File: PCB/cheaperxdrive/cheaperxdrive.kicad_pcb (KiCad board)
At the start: 2 copper layers, 20 parts, among them Q1 JMSL0302AG, Q2 JMSL0302AG, Q3 JMSL0302AG, Q4 JMSL0302AG, Q5 JMSL0302AG, Q6 JMSL0302AG, Q7 JMSL0302AG, Q8 JMSL0302AG, U1 STM32F405RGTx, U2 LM5109BMA, U3 DRV8301, U4 AS5047D, U5 SN65HVD232, U6 LP5907MFX-3.3, U7 AMS1117-3.3

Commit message: started schematic
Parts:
- added C1: 12p, Capacitor_SMD:C_0201_0603Metric, F.Cu at (80.6, 133.0)
- added C10: 2u2, Capacitor_SMD:C_0201_0603Metric, F.Cu at (80.6, 148.7)
- added C11: 2n2, Capacitor_SMD:C_0201_0603Metric, F.Cu at (83.0, 133.0)
- added C12: 2n2, Capacitor_SMD:C_0201_0603Metric, F.Cu at (83.0, 134.7)
- added C13: 22n, Capacitor_SMD:C_0201_0603Metric, F.Cu at (83.0, 136.5)
- added C14: 100n, Capacitor_SMD:C_0201_0603Metric, F.Cu at (83.0, 138.2)
- added C15: 100n, Capacitor_SMD:C_0201_0603Metric, F.Cu at (83.0, 140.0)
- added C16: 4u7, Capacitor_SMD:C_0201_0603Metric, F.Cu at (83.0, 141.7)
- added C17: 100n, Capacitor_SMD:C_0201_0603Metric, F.Cu at (83.0, 143.5)
- added C18: 100n, Capacitor_SMD:C_0201_0603Metric, F.Cu at (83.0, 145.2)
- added C19: 100n, Capacitor_SMD:C_0201_0603Metric, F.Cu at (83.0, 147.0)
- added C2: 12p, Capacitor_SMD:C_0201_0603Metric, F.Cu at (80.6, 134.7)
- added C20: 270p, Capacitor_SMD:C_0201_0603Metric, F.Cu at (83.0, 148.7)
- added C21: 270p, Capacitor_SMD:C_0201_0603Metric, F.Cu at (85.5, 133.0)
- added C22: 100n, Capacitor_SMD:C_0201_0603Metric, F.Cu at (85.5, 134.7)
- added C23: 4u7, Capacitor_SMD:C_0201_0603Metric, F.Cu at (85.5, 136.5)
- added C24: 12p, Capacitor_SMD:C_0201_0603Metric, F.Cu at (85.5, 138.2)
- added C25: 100n, Capacitor_SMD:C_0201_0603Metric, F.Cu at (85.5, 140.0)
- added C26: 2u2, Capacitor_SMD:C_0201_0603Metric, F.Cu at (85.5, 141.7)
- added C27: 100n, Capacitor_SMD:C_0201_0603Metric, F.Cu at (85.5, 143.5)
- added C28: 100n, Capacitor_SMD:C_0201_0603Metric, F.Cu at (85.5, 145.2)
- added C29: 4u7, Capacitor_SMD:C_0201_0603Metric, F.Cu at (85.5, 147.0)
- added C3: 2u2, Capacitor_SMD:C_0201_0603Metric, F.Cu at (80.6, 136.5)
- added C30: 2u2, Capacitor_SMD:C_0201_0603Metric, F.Cu at (85.5, 148.7)
- added C31: 4u7, Capacitor_SMD:C_0201_0603Metric, F.Cu at (87.9, 133.0)
- added C32: 4u7, Capacitor_SMD:C_0201_0603Metric, F.Cu at (87.9, 134.7)
- added C33: 100u, Capacitor_THT:CP_Radial_D5.0mm_P2.50mm, F.Cu at (64.7, 135.4)
- added C34: 100u, Capacitor_THT:CP_Radial_D5.0mm_P2.50mm, F.Cu at (64.7, 141.9)
- added C35: 100u, Capacitor_THT:CP_Radial_D5.0mm_P2.50mm, F.Cu at (64.7, 148.5)
- added C36: 100u, Capacitor_THT:CP_Radial_D5.0mm_P2.50mm, F.Cu at (64.7, 155.0)
- added C37: 100u, Capacitor_THT:CP_Radial_D5.0mm_P2.50mm, F.Cu at (64.7, 161.6)
- added C38: 4u7, Capacitor_SMD:C_0201_0603Metric, F.Cu at (87.9, 136.5)
- added C39: 4u7, Capacitor_SMD:C_0201_0603Metric, F.Cu at (87.9, 138.2)
- added C4: 2u2, Capacitor_SMD:C_0201_0603Metric, F.Cu at (80.6, 138.2)
- added C40: 4u7, Capacitor_SMD:C_0201_0603Metric, F.Cu at (87.9, 140.0)
- added C41: 2u2, Capacitor_SMD:C_0201_0603Metric, F.Cu at (87.9, 141.7)
- added C42: 100n, Capacitor_SMD:C_0201_0603Metric, F.Cu at (87.9, 143.5)
- added C43: 2u2, Capacitor_SMD:C_0201_0603Metric, F.Cu at (87.9, 145.2)
- added C44: 100n, Capacitor_SMD:C_0201_0603Metric, F.Cu at (87.9, 147.0)
- added C45: 2u2, Capacitor_SMD:C_0201_0603Metric, F.Cu at (87.9, 148.7)
- added C46: 100n, Capacitor_SMD:C_0201_0603Metric, F.Cu at (90.4, 133.0)
- added C5: 100p, Capacitor_SMD:C_0201_0603Metric, F.Cu at (80.6, 140.0)
- added C6: 270p, Capacitor_SMD:C_0201_0603Metric, F.Cu at (80.6, 141.7)
- added C7: 22n, Capacitor_SMD:C_0201_0603Metric, F.Cu at (80.6, 143.5)
- added C8: 2u2, Capacitor_SMD:C_0201_0603Metric, F.Cu at (80.6, 145.2)
- added C9: 2u2, Capacitor_SMD:C_0201_0603Metric, F.Cu at (80.6, 147.0)
- added D1: DSK310, Capacitor_SMD:C_0201_0603Metric, F.Cu at (90.4, 134.7)
- added D2: DSK310, Capacitor_SMD:C_0201_0603Metric, F.Cu at (90.4, 136.5)
- added D3: DSK310, Capacitor_SMD:C_0201_0603Metric, F.Cu at (90.4, 138.2)
- added D4: DSK310, Capacitor_SMD:C_0201_0603Metric, F.Cu at (90.4, 140.0)
- added D5: DSK310, Capacitor_SMD:C_0201_0603Metric, F.Cu at (90.4, 141.7)
- added H10: MountingHole, MountingHole:MountingHole_3.2mm_M3, F.Cu at (240.3, 70.5)
- added H11: MountingHole, MountingHole:MountingHole_3.2mm_M3, F.Cu at (184.2, 96.0)
- added H12: MountingHole, MountingHole:MountingHole_3.2mm_M3, F.Cu at (184.2, 70.5)
- added H13: MountingHole, MountingHole:MountingHole_3.2mm_M3, F.Cu at (240.3, 96.0)
- added H6: MountingHole_Pad, MountingHole:MountingHole_4.3mm_M4_Pad_Via, F.Cu at (74.3, 137.2)
- added H7: MountingHole_Pad, MountingHole:MountingHole_4.3mm_M4_Pad_Via, F.Cu at (74.3, 147.3)
- added H8: MountingHole, MountingHole:MountingHole_3.2mm_M3, F.Cu at (240.3, 121.5)
- added H9: MountingHole, MountingHole:MountingHole_3.2mm_M3, F.Cu at (184.2, 121.5)
- added J2: Conn_01x05, Connector_JST:JST_EH_B5B-EH-A_1x05_P2.50mm_Vertical, F.Cu at (108.9, 96.8)
- added J3: Conn_01x02, Connector_JST:JST_XH_B2B-XH-AM_1x02_P2.50mm_Vertical, F.Cu at (72.7, 155.8)
- added J4: Conn_01x02_Pin, Connector_PinHeader_2.54mm:PinHeader_1x02_P2.54mm_Vertical, F.Cu at (107.7, 108.2)
- added J5: Conn_01x05, Connector_JST:JST_EH_B6B-EH-A_1x06_P2.50mm_Vertical, F.Cu at (108.9, 102.7)
- added L1: 22u, Inductor_SMD:L_0201_0603Metric, F.Cu at (139.4, 74.2)
- added P1: USB_C_Plug_USB2.0, Connector_USB:USB_C_Receptacle_HRO_TYPE-C-31-M-12, F.Cu at (187.4, 108.9)
- added R1: 220k, Resistor_SMD:R_0201_0603Metric, F.Cu at (139.4, 76.0)
- added R10: 10k, Resistor_SMD:R_0201_0603Metric, F.Cu at (141.8, 77.7)
- added R11: 2R2, Resistor_SMD:R_0201_0603Metric, F.Cu at (141.8, 79.5)
- added R12: 2R2, Resistor_SMD:R_0201_0603Metric, F.Cu at (141.8, 81.2)
- added R13: 0m5, Resistor_SMD:R_0201_0603Metric, F.Cu at (141.8, 83.0)
- added R14: 2R2, Resistor_SMD:R_0201_0603Metric, F.Cu at (141.8, 84.7)
- added R15: 2R2, Resistor_SMD:R_0201_0603Metric, F.Cu at (141.8, 86.5)
- added R16: 0m5, Resistor_SMD:R_0201_0603Metric, F.Cu at (144.3, 74.2)
- added R17: 2R2, Resistor_SMD:R_0201_0603Metric, F.Cu at (144.3, 76.0)
- added R18: 2R2, Resistor_SMD:R_0201_0603Metric, F.Cu at (144.3, 77.7)
- added R19: 3k3, Resistor_SMD:R_0201_0603Metric, F.Cu at (144.3, 79.5)
- added R2: 18k, Resistor_SMD:R_0201_0603Metric, F.Cu at (139.4, 77.7)
- added R20: 2R2, Resistor_SMD:R_0201_0603Metric, F.Cu at (144.3, 81.2)
- added R21: 2R2, Resistor_SMD:R_0201_0603Metric, F.Cu at (144.3, 83.0)
- added R22: 3k3, Resistor_SMD:R_0201_0603Metric, F.Cu at (144.3, 84.7)
- added R23: 3k3, Resistor_SMD:R_0201_0603Metric, F.Cu at (144.3, 86.5)
- added R24: 3k3, Resistor_SMD:R_0201_0603Metric, F.Cu at (146.7, 74.2)
- added R25: 3k3, Resistor_SMD:R_0201_0603Metric, F.Cu at (146.7, 76.0)
- added R26: 3k3, Resistor_SMD:R_0201_0603Metric, F.Cu at (146.7, 77.7)
- added R27: 3k3, Resistor_SMD:R_0201_0603Metric, F.Cu at (146.7, 79.5)
- added R28: 3k3, Resistor_SMD:R_0201_0603Metric, F.Cu at (146.7, 81.2)
- added R29: 120, Resistor_SMD:R_0201_0603Metric, F.Cu at (146.7, 83.0)
- added R3: 18k, Resistor_SMD:R_0201_0603Metric, F.Cu at (139.4, 79.5)
- added R30: 5K1, Resistor_SMD:R_0201_0603Metric, F.Cu at (146.7, 84.7)
- added R31: 5K1, Resistor_SMD:R_0201_0603Metric, F.Cu at (146.7, 86.5)
- added R4: 3k3, Resistor_SMD:R_0201_0603Metric, F.Cu at (139.4, 81.2)
- added R5: 47k, Resistor_SMD:R_0201_0603Metric, F.Cu at (139.4, 83.0)
- added R6: 22, Resistor_SMD:R_0201_0603Metric, F.Cu at (139.4, 84.7)
- added R7: 22, Resistor_SMD:R_0201_0603Metric, F.Cu at (139.4, 86.5)
- added R8: 47k, Resistor_SMD:R_0201_0603Metric, F.Cu at (141.8, 74.2)
- added R9: 47k, Resistor_SMD:R_0201_0603Metric, F.Cu at (141.8, 76.0)
- added SW1: TS-1187A, Button_Switch_SMD:SW_SPST_CK_RS282G05A3, F.Cu at (153.4, 92.0)
- added TP1: TestPoint, TestPoint:TestPoint_Pad_D2.5mm, F.Cu at (160.4, 106.8)
- added TP2: TestPoint, TestPoint:TestPoint_Pad_D2.5mm, F.Cu at (160.4, 111.3)
- added TP3: TestPoint, TestPoint:TestPoint_Pad_D2.5mm, F.Cu at (160.4, 115.9)
- added U10: LM5109BMA, Package_SO:SOIC-8_3.9x4.9mm_P1.27mm, F.Cu at (101.2, 110.7)
- added U11: L7812, L8712:78XXS, F.Cu at (153.8, 84.6)
- added U12: USBLC6-2SC6, Package_TO_SOT_SMD:SOT-23-6, F.Cu at (134.0, 66.1)
- added U8: LM5109BMA, Package_SO:SOIC-8_3.9x4.9mm_P1.27mm, F.Cu at (101.2, 97.6)
- added U9: LM5109BMA, Package_SO:SOIC-8_3.9x4.9mm_P1.27mm, F.Cu at (101.2, 104.2)
- added Y1: 24M, Crystal:Crystal_SMD_3225-4Pin_3.2x2.5mm, F.Cu at (120.9, 110.0)
- moved H1 52.6 mm to (62.4, 119.1)
- moved H2 52.6 mm to (52.4, 119.1)
- moved H3 52.6 mm to (42.4, 119.1)
- moved H4 52.6 mm to (32.4, 119.1)
- moved H5 52.6 mm to (81.5, 108.7)
- moved Q1 52.6 mm to (62.4, 106.0)
- moved Q2 52.6 mm to (62.4, 111.7)
- moved Q3 52.6 mm to (52.4, 106.0)
- moved Q4 52.6 mm to (52.4, 111.7)
- moved Q5 52.6 mm to (42.4, 106.0)
- moved Q6 52.6 mm to (42.4, 111.7)
- moved Q7 52.6 mm to (32.4, 106.0)
- moved Q8 52.6 mm to (32.4, 111.7)
- moved U1 52.6 mm to (63.4, 84.0)
- moved U4 52.6 mm to (49.9, 95.9)
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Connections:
- U1 pad 12: unconnected-(U1-VSSA-Pad12) -> GND
- U1 pad 17: unconnected-(U1-PA3-Pad17) -> /GPIO4
- U1 pad 18: Net-(U1-VSS-Pad18) -> GND
- U1 pad 63: Net-(U1-VSS-Pad18) -> GND
- U1 pad 7: Net-(U1-NRST) -> /SYS_RST
- U5 pad 3: Net-(U5-VCC) -> +3V3
- U5 pad 6: unconnected-(U5-CANL-Pad6) -> /CAN_L
- U5 pad 7: unconnected-(U5-CANH-Pad7) -> /CAN_H
- U7 pad 3: unconnected-(U7-VI-Pad3) -> +5V
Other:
- board outline added: 63 x 58 mm

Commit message: finished first layer, may rework
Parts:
- C1, C10, C11, C12, C13, C14, C15, C16, C17, C18, C19, C2, C20, C21, C22, C23, C24, C27, C3, C4, C5, C6, C8, C9, D1, L1, R1, R19, R22, R3, R5, R8, R9, U1, U10, U2, U3, U4, U8, U9, Y1: moved to B.Cu
- moved H4 206.3 mm to (237.8, 99.3)
- moved Q8 195.3 mm to (226.8, 92.1)
- moved Q7 191.3 mm to (222.5, 84.6)
- moved H7 173.9 mm to (231.9, 73.7), turned to 90 degrees
- moved U3 168.3 mm to (200.5, 87.0), turned to -90 degrees
- moved C33 163.5 mm to (224.4, 100.6), turned to -90 degrees
- moved U4 162.4 mm to (212.3, 96.0), turned to 180 degrees
- moved H6 160.5 mm to (221.8, 73.7), turned to 90 degrees
- moved U1 158.9 mm to (222.3, 86.3), turned to 180 degrees
- moved C34 158.7 mm to (217.9, 100.6), turned to -90 degrees
- moved H5 157.6 mm to (237.8, 87.9)
- moved Q1 156.6 mm to (218.4, 92.2), turned to 0 degrees
- moved Q3 156.6 mm to (208.4, 92.2), turned to 0 degrees
- moved Q5 156.6 mm to (198.4, 92.2), turned to 0 degrees
- moved H1 156.5 mm to (212.2, 73.7)
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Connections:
- H6 pad 1: VDD -> VPP
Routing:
- net VPP: track 0.00 -> 126.5 mm
- net GND: track 0.00 -> 104.4 mm, vias 0 -> 7
- net /0SH_A: track 0.00 -> 26.3 mm, vias 0 -> 1
- net /0SH_C: track 0.00 -> 24.1 mm, vias 0 -> 1
- net /0SH_B: track 0.00 -> 23.9 mm, vias 0 -> 1
- net /USB_VBUS: track 0.00 -> 23.4 mm
- net /USB_P: track 0.00 -> 19.8 mm
- net +5V: track 0.00 -> 18.4 mm, vias 0 -> 1
- net /SH_AUX: track 0.00 -> 18.1 mm
- net +3V3: track 0.00 -> 17.7 mm, vias 0 -> 1
- net /CAN_L: track 0.00 -> 17.5 mm
- net /USB_N: track 0.00 -> 15.9 mm
- net /CAN_H: track 0.00 -> 13.8 mm
- net Net-(P1-CC1): track 0.00 -> 10.2 mm
- net Net-(P1-CC2): track 0.00 -> 9.28 mm
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- added copper zone on F.Cu, net GND

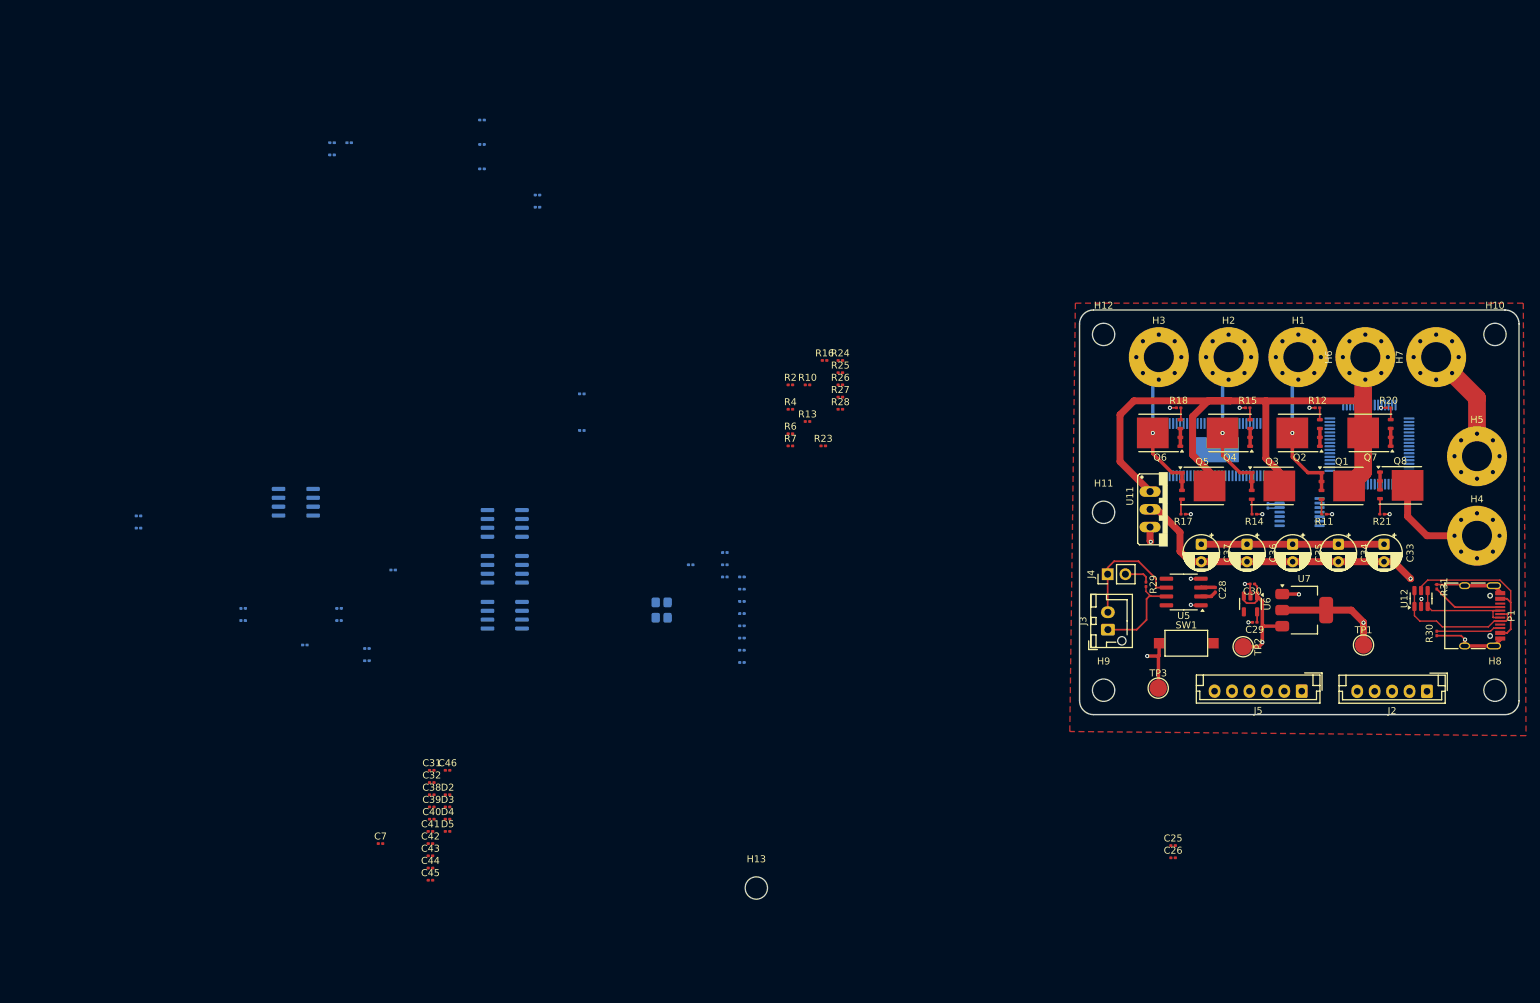
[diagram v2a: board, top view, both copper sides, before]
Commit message: pausing pcb work for now, corrected schematic to remove redundant gate drivers and removed 5v ldo
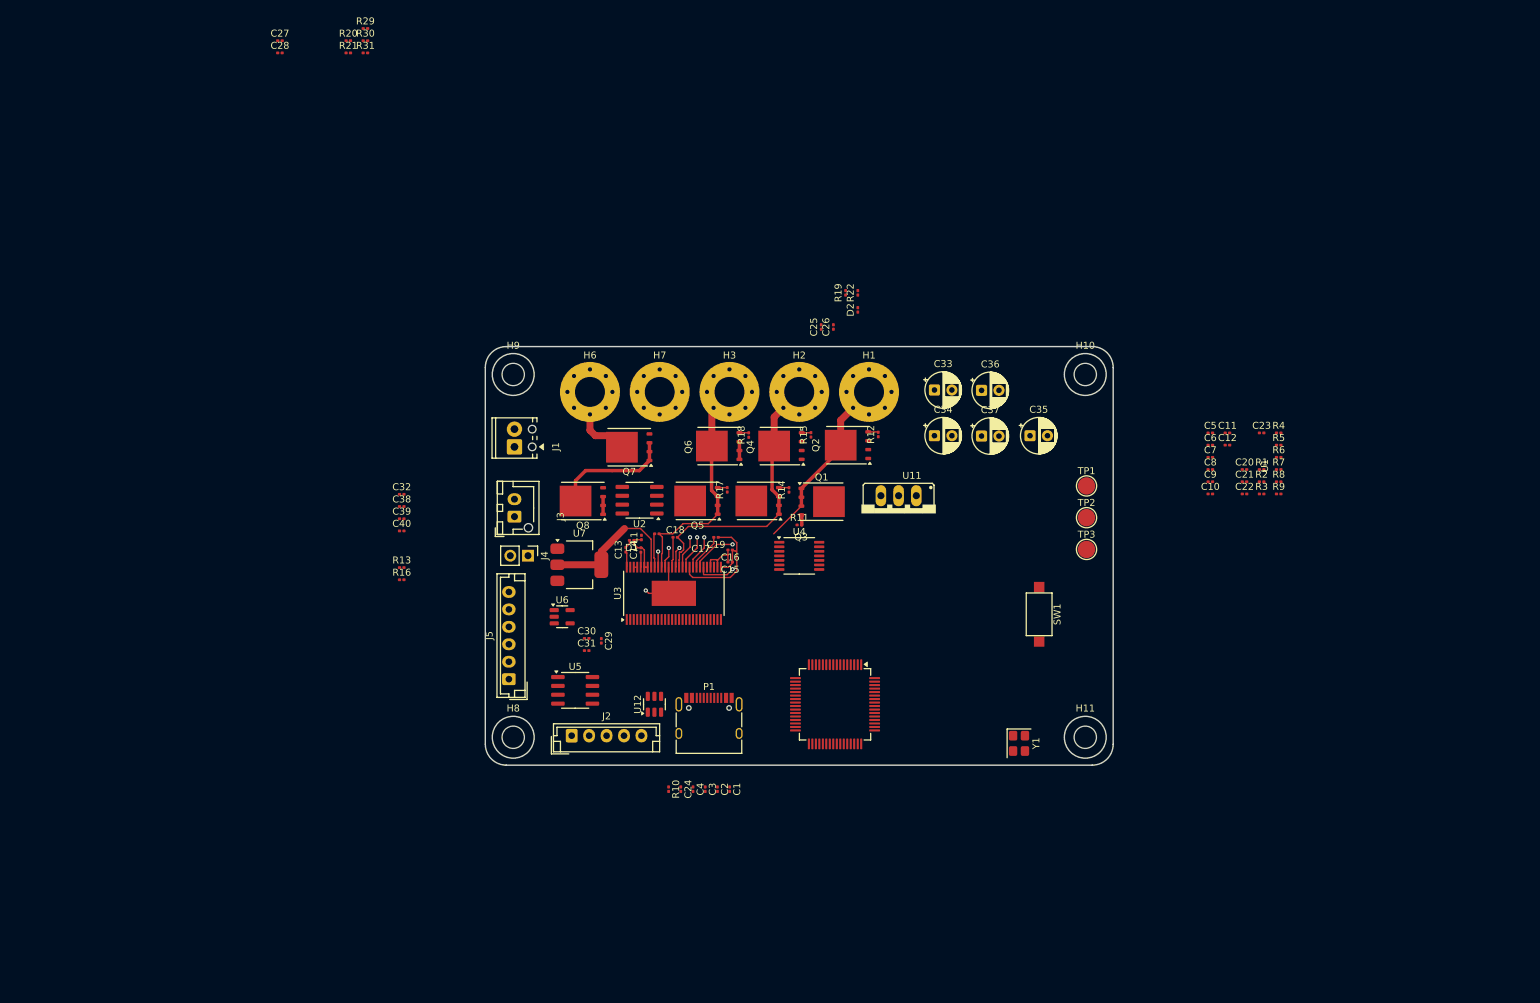
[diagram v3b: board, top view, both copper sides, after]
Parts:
- removed C41, C43, C45: 2u2, Capacitor_SMD:C_0201_0603Metric
- removed C42, C44, C46: 100n, Capacitor_SMD:C_0201_0603Metric
- removed D3, D4, D5: DSK310, Capacitor_SMD:C_0201_0603Metric
- removed H12, H13: MountingHole, MountingHole:MountingHole_3.2mm_M3
- removed H4, H5: MountingHole_Pad, MountingHole:MountingHole_4.3mm_M4_Pad_Via
- removed R23, R24, R25, R26, R27, R28: 3k3, Resistor_SMD:R_0201_0603Metric
- removed U10, U8, U9: LM5109BMA, Package_SO:SOIC-8_3.9x4.9mm_P1.27mm
- added J1: Screw_Terminal_01x02, TerminalBlock_Phoenix:TerminalBlock_Phoenix_MPT-0,5-2-2.54_1x02_P2.54mm_Horizontal, F.Cu at (99.8, 86.6)
- C1, C10, C11, C12, C13, C14, C15, C16, C17, C18, C19, C2, C20, C21, C22, C23, C24, C27, C3, C4, C5, C6, C8, C9, D1, L1, R1, R19, R22, R3, R5, R8, R9, U1, U2, U3, U4, Y1: moved to F.Cu
- moved R30 175.5 mm to (78.4, 28.4), turned to 0 degrees
- moved R31 171.6 mm to (78.4, 30.1), turned to 0 degrees
- moved R21 162.3 mm to (76.0, 30.1), turned to 0 degrees
- moved R20 158.1 mm to (76.0, 28.4)
- moved C27 156.5 mm to (66.2, 28.4), turned to 0 degrees
- moved C28 154.6 mm to (66.2, 30.1), turned to 0 degrees
- moved C10 153.7 mm to (199.5, 93.3), turned to 0 degrees
- moved C9 153.7 mm to (199.5, 91.6), turned to 0 degrees
- moved R8 144.1 mm to (209.3, 91.6), turned to 0 degrees
- moved R9 144.1 mm to (209.3, 93.3), turned to 0 degrees
- moved H8 140.9 mm to (99.6, 128.2)
- moved R29 137.4 mm to (78.4, 26.6), turned to 0 degrees
- moved C7 131.2 mm to (199.5, 88.1)
- moved C11 127.2 mm to (202.0, 84.6), turned to 0 degrees
- moved C12 127.2 mm to (202.0, 86.3), turned to 0 degrees
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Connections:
- R8 pad 2: /S1_N -> /0SL_B
- R9 pad 2: /S2_N -> /0SL_C
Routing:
- net VPP: track 126.5 -> 15.7 mm
- net GND: track 104.4 -> 21.2 mm, vias 7 -> 1
- net /USB_VBUS: track 23.4 -> 0.00 mm
- net /USB_P: track 19.8 -> 0.00 mm
- net +5V: track 18.4 -> 0.00 mm, vias 1 -> 0
- net /CAN_L: track 17.5 -> 0.00 mm
- net /0SH_B: track 23.9 -> 40.5 mm, vias 1 -> 0
- net /USB_N: track 15.9 -> 0.00 mm
- net Net-(U3-BST_C): track 0.00 -> 15.4 mm
- net /CAN_H: track 13.8 -> 0.00 mm
- net Net-(P1-CC1): track 10.2 -> 0.00 mm
- net Net-(P1-CC2): track 9.28 -> 0.00 mm
- net /0SH_C: track 24.1 -> 31.3 mm, vias 1 -> 0
- net /0SH_A: track 26.3 -> 33.5 mm, vias 1 -> 0
- net Net-(D1-K): track 0.00 -> 6.46 mm
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- removed copper zone on F.Cu, net GND
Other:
- board size 63 x 58 mm -> 90 x 60 mm
